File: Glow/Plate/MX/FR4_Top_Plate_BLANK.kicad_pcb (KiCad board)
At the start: 2 copper layers, 139.1 x 107.7 mm, 34 parts, among them SW1 SW_PUSH, SW10 SW_PUSH, SW11 SW_PUSH, SW12 SW_PUSH, SW13 SW_PUSH, SW14 SW_PUSH, SW15 SW_PUSH, SW16 SW_PUSH, SW17 SW_PUSH, SW18 SW_PUSH, SW19 SW_PUSH, SW2 SW_PUSH, SW20 SW_PUSH, SW21 SW_PUSH, SW22 SW_PUSH, SW23 SW_PUSH, SW24 SW_PUSH, SW25 SW_PUSH, SW26 SW_PUSH, SW27 SW_PUSH, SW28 SW_PUSH, SW29 SW_PUSH, SW3 SW_PUSH, SW4 SW_PUSH, SW5 SW_PUSH, SW6 SW_PUSH, SW7 SW_PUSH, SW8 SW_PUSH, SW9 SW_PUSH

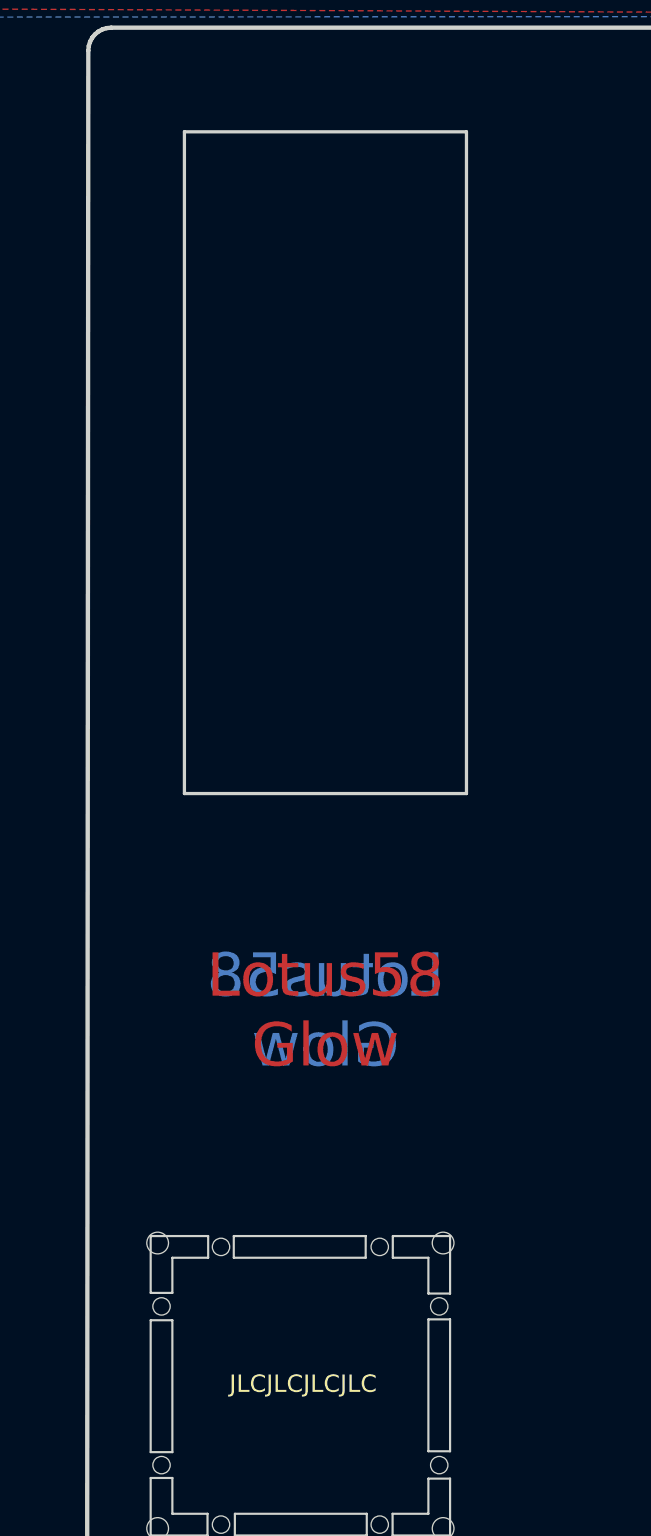
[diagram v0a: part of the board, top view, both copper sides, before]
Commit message: Blank front plate option added
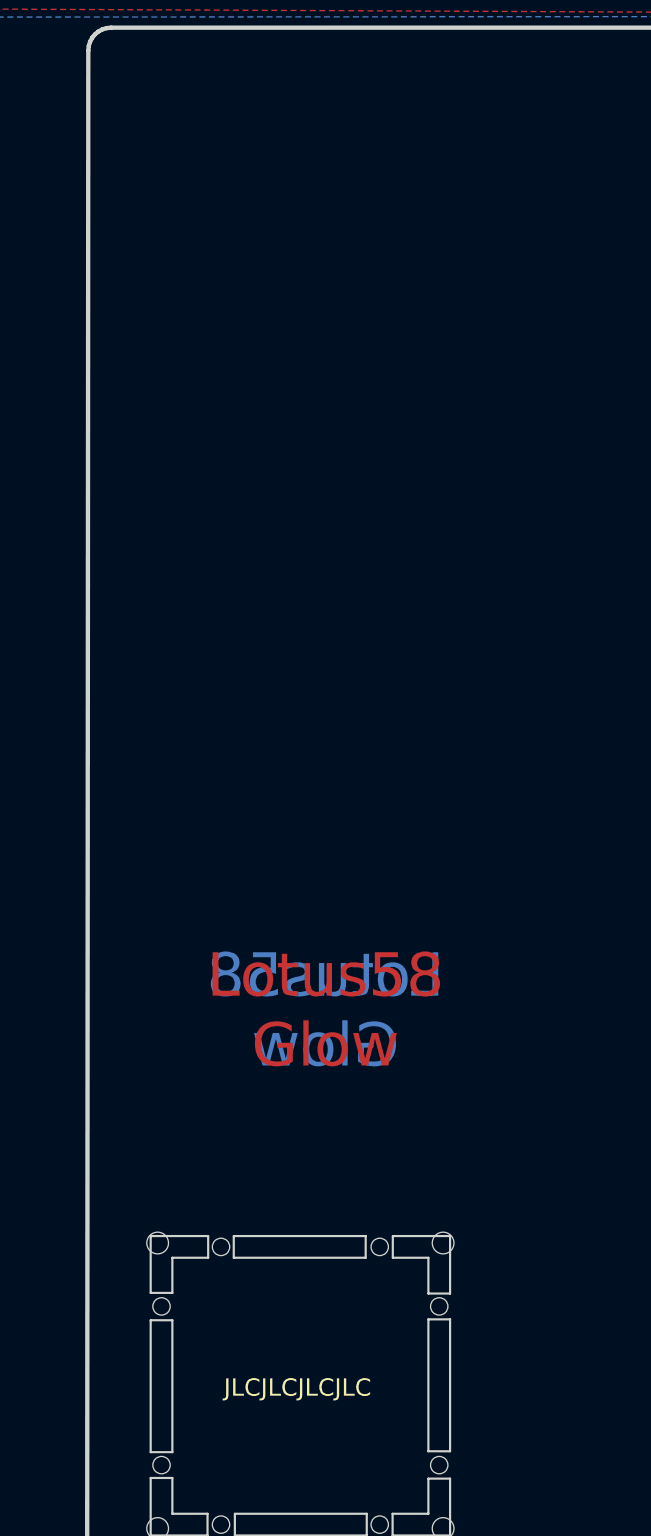
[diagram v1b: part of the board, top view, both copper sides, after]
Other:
- outline, holes or cut-outs redrawn

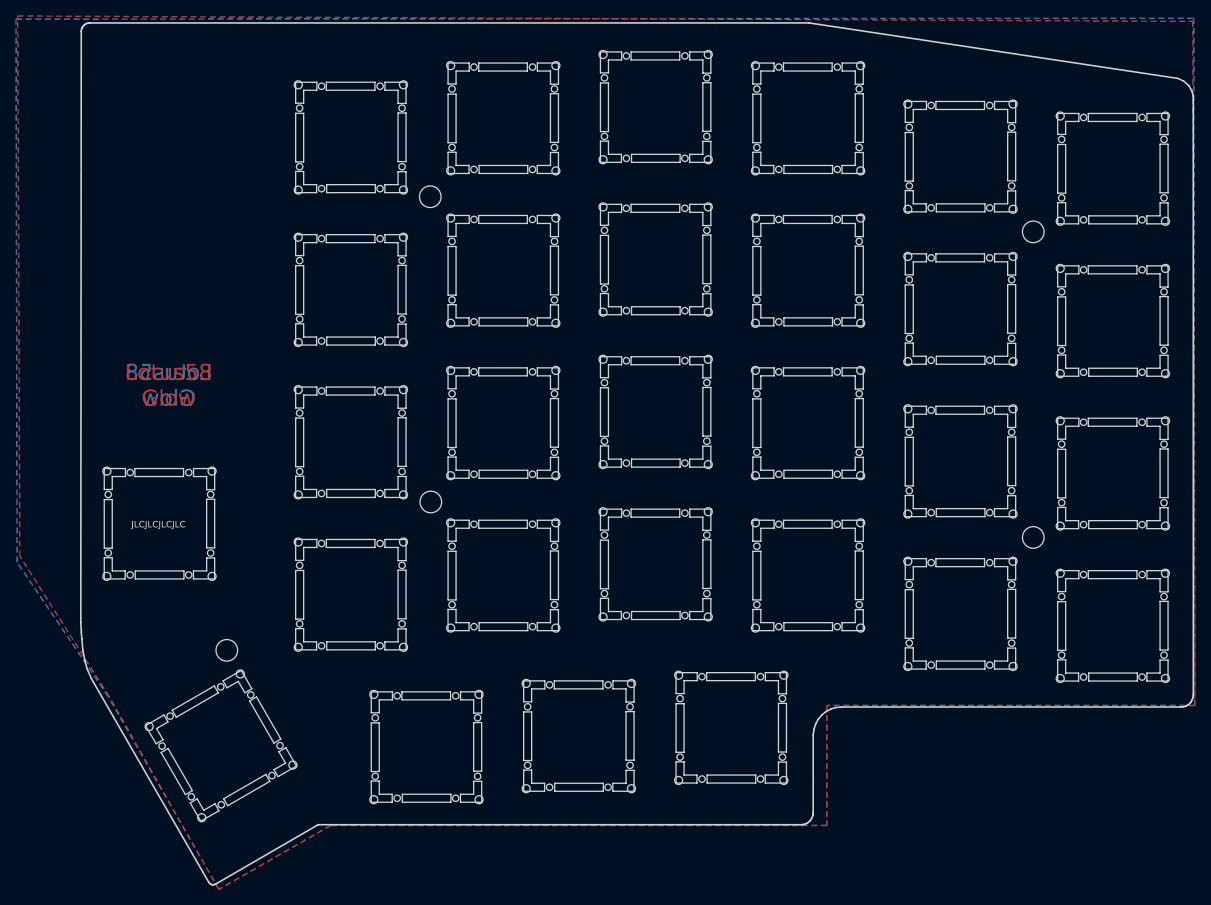
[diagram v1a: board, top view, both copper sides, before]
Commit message: Updated plates to remove break-away parts
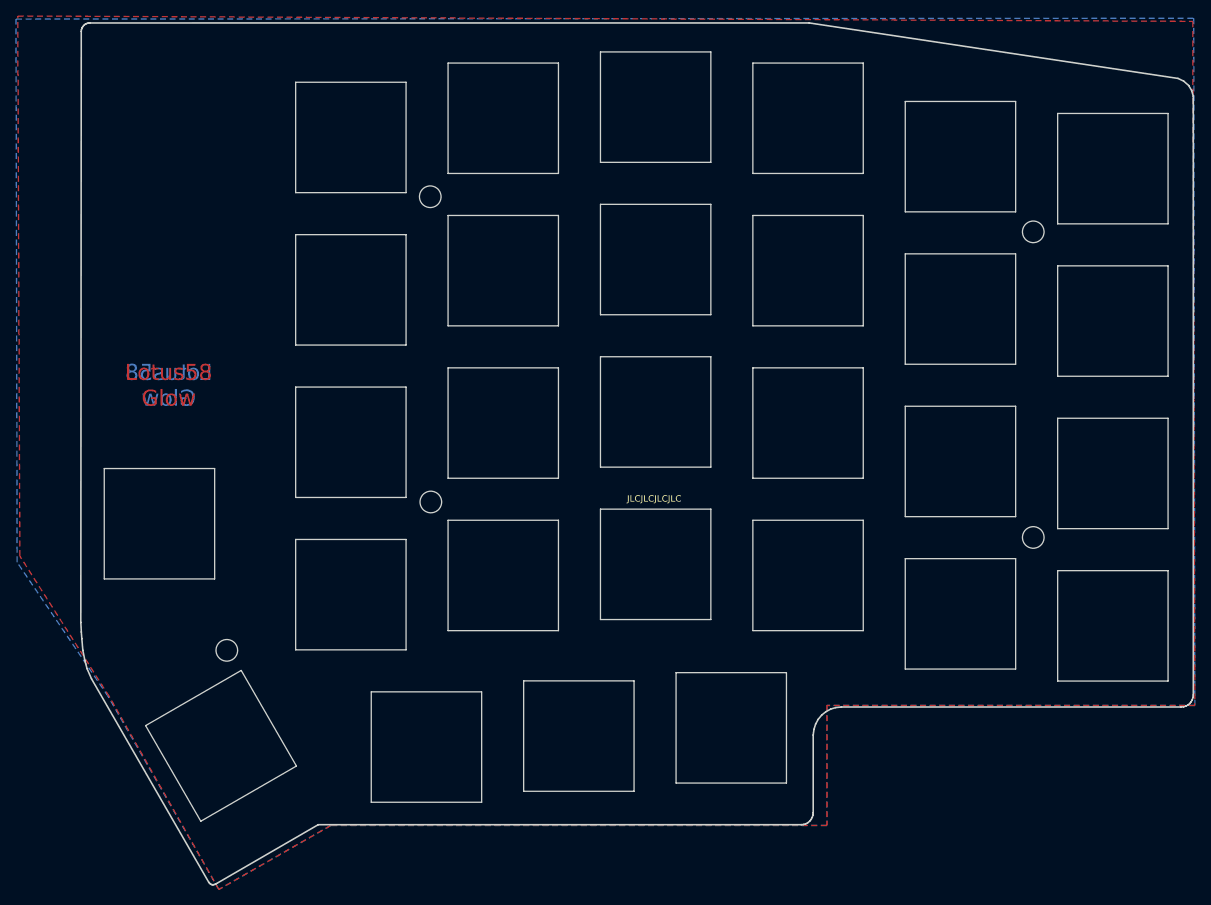
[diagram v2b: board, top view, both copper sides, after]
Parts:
- SW1, SW10, SW11, SW12, SW13, SW14, SW15, SW16, SW17, SW18, SW19, SW2, SW20, SW21, SW22, SW23, SW24, SW25, SW26, SW27, SW28, SW29, SW3, SW4, SW5, SW6, SW7, SW8, SW9: footprint Keyboard Library:Cherry_MX_Plate_Hole_Breakoff -> Keyboard Library:Cherry_MX_Plate_Hole_Placeholder
